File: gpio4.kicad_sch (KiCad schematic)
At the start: 4 parts, among them U27 RK3576

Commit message: Add files via upload
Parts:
- renumbered C330 to C102, C331 to C103, C332 to C104, U27 to U2

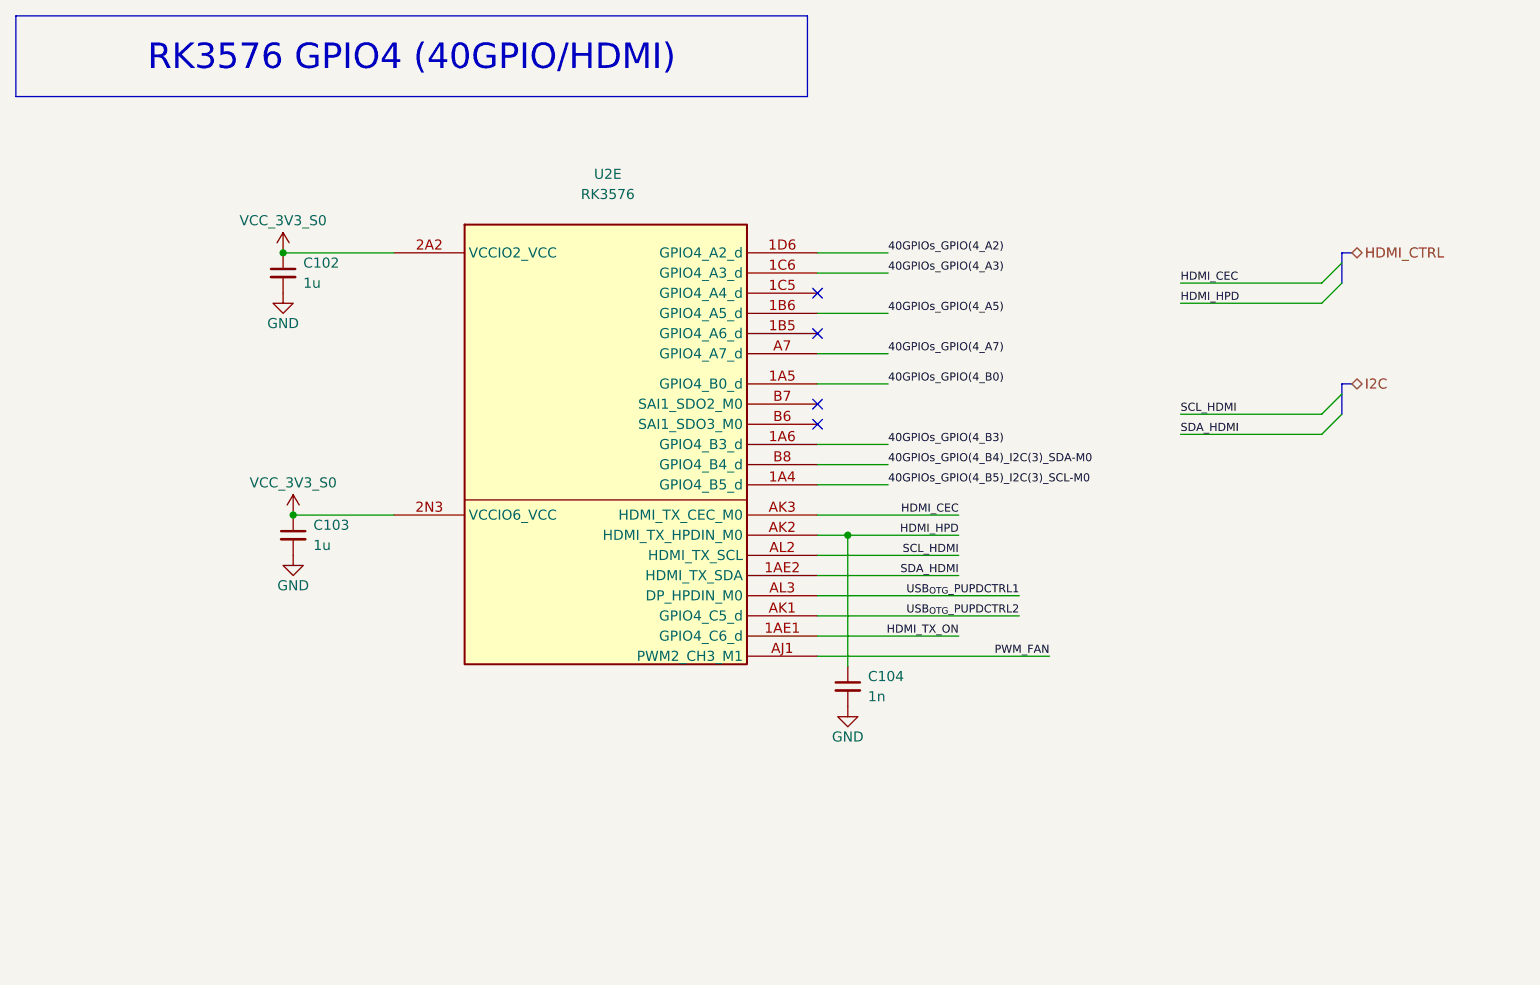
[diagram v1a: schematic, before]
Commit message: SBC Board V0.2
The SBC schematics before footprint and part number check
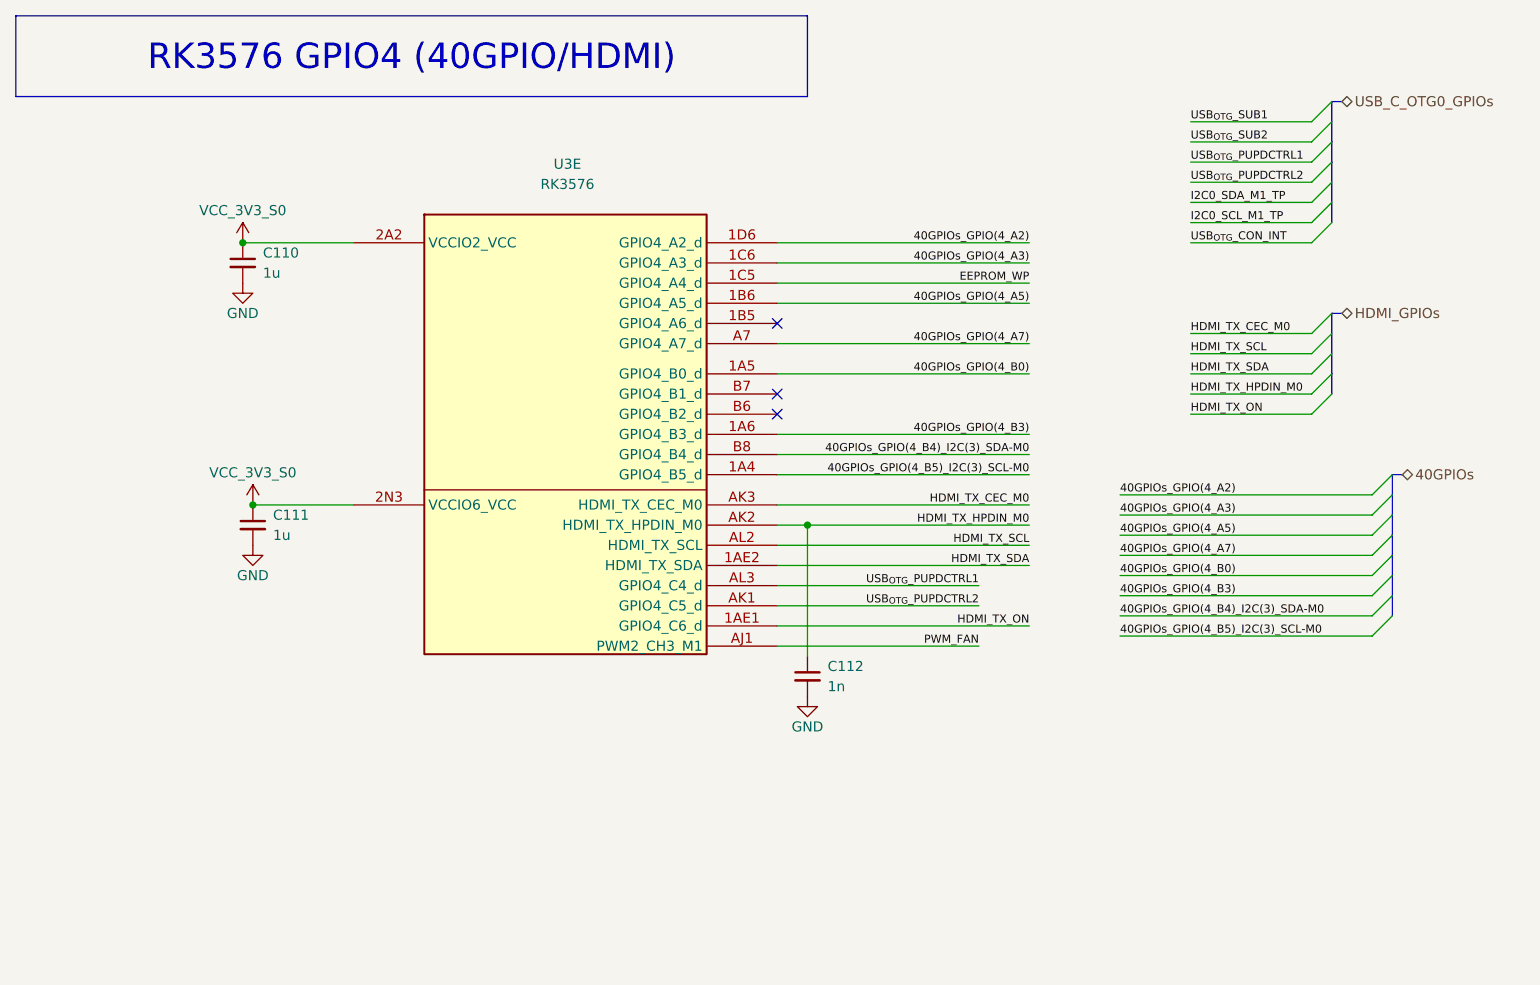
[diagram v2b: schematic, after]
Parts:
- U3: renamed from U2; footprint (none) -> easyeda2kicad:FCCSP-698_L17.2-W16.1-TL_RK3576
- renumbered C102 to C110, C103 to C111, C104 to C112
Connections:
- net EEPROM_WP: now reaches U3.1C5 (SAI4_SCLK_M0)
- net HDMI_CEC renamed HDMI_TX_CEC_M0
- net HDMI_HPD renamed HDMI_TX_HPDIN_M0
- net SCL_HDMI renamed HDMI_TX_SCL
- net SDA_HDMI renamed HDMI_TX_SDA
- no-connect marks 4 -> 3
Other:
- moved on the sheet: C110, C111, C112, U3E

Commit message: SBCv0.3
there is no big thing update just some LCSC & Mouser parts
and Big problem deleted alot of component values (:
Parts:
- removed C112: 1n, Capacitor_SMD:C_0402_1005Metric_Pad0.74x0.62mm_HandSolder, symbol New_Library_0:C_Small_edited
- added C398: 10n, Capacitor_SMD:C_0201_0603Metric_Pad0.64x0.40mm_HandSolder, symbol New_Library_0:C_Small_edited
- C110, C111: footprint Capacitor_SMD:C_0402_1005Metric_Pad0.74x0.62mm_HandSolder -> Capacitor_SMD:C_0201_0603Metric_Pad0.64x0.40mm_HandSolder; LCSC Part (none) -> C5209398; Mouser Part (none) -> CL03A105KP3NSNC
- U3: value RK3576 -> (none); LCSC Part (none) -> (polyline
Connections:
- net GND: now also C398.2
- net HDMI_TX_HPDIN_M0: now also C398.1
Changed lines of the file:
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@@
-	)
-	(symbol
-		(lib_id "New_Library_0:C_Small_edited")
-		(at 111.76 95.25 0)
-		(unit 1)
-		(body_style 1)
-		(exclude_from_sim no)
-		(in_bom yes)
-		(on_board yes)
-		(in_pos_files yes)
-		(dnp no)
-		(fields_autoplaced yes)
-		(property "Reference" "C112"
-			(at 114.3 93.9862 0)
-			(show_name no)
-			(do_not_autoplace no)
-			(effects
-				(font
-					(size 1.27 1.27)
-				)
-				(justify left)
-			)
-		)
-		(property "Value" "1n"
-			(at 114.3 96.5262 0)
-			(show_name no)
-			(do_not_autoplace no)
-			(effects
-				(font
-					(size 1.27 1.27)
-				)
-				(justify left)
-			)
-		)
-		(property "Footprint" "Capacitor_SMD:C_0402_1005Metric_Pad0.74x0.62mm_HandSolder"
-			(at 111.76 95.25 0)
-			(hide yes)
-			(show_name no)
-			(do_not_autoplace no)
-			(effects
-				(font
-					(size 1.27 1.27)
-				)
-			)
-		)
-		(property "Datasheet" ""
-			(at 111.76 95.25 0)
-			(hide yes)
-			(show_name no)
-			(do_not_autoplace no)
-			(effects
-				(font
-					(size 1.27 1.27)
-				)
-			)
-		)
-		(property "Description" "Unpolarized capacitor, small symbol"
-			(at 111.76 95.25 0)
-			(hide yes)
-			(show_name no)
-			(do_not_autoplace no)
-			(effects
-				(font
-					(size 1.27 1.27)
-				)
-			)
-		)
-		(property "Dielectric" ""
-			(at 111.76 95.25 0)
-			(hide yes)
-			(show_name no)
-			(do_not_autoplace no)
-			(effects
-				(font
-					(size 1.27 1.27)
-				)
-			)
-		)
-		(property "Voltage" ""
-			(at 111.76 95.25 0)
-			(hide yes)
-			(show_name no)
-			(do_not_autoplace no)
-			(effects
-				(font
-					(size 1.27 1.27)
-				)
-			)
-		)
-		(property "KLC_S3.3" ""
-			(at 111.76 95.25 0)
-			(hide yes)
-			(show_name no)
-			(do_not_autoplace no)
-			(effects
-				(font
-					(size 1.27 1.27)
-				)
-			)
-		)
-		(property "KLC_S4.1" ""
-			(at 111.76 95.25 0)
-			(hide yes)
-			(show_name no)
-			(do_not_autoplace no)
-			(effects
-				(font
-					(size 1.27 1.27)
-				)
-			)
-		)
-		(property "KLC_S5.1" ""
-			(at 111.76 95.25 0)
-			(hide yes)
-			(show_name no)
-			(do_not_autoplace no)
-			(effects
-				(font
-					(size 1.27 1.27)
-				)
-			)
-		)
-		(pin "1"
-		)
-		(pin "2"
-		)
-		(instances
-			(project "RK3576 SBC"
-				(path "/b79dbff4-0cad-4ff7-bec2-7c0e4f8b14d3/34f9b0cb-aeae-42b4-a2af-a0a79afcf392/3a63a63f-0660-4de2-bd2e-c637401ccb58"
-					(reference "C112")
-					(unit 1)
-				)
-			)
-		)
 	)
 	(symbol
@@
 			)
 		)
-		(property "Value" "RK3576"
+		(property "Value" ""
 			(at 81.534 33.274 0)
 			(show_name no)
@@
 			)
 		)
-		(property "KLC_S5.1" ""
+		(property "LCSC Part" "(polyline"
+			(at 81.28 64.77 0)
+			(hide yes)
+			(show_name no)
+			(do_not_autoplace no)
+			(effects
+				(font
+					(size 1.27 1.27)
+				)
+			)
+		)
+		(property "KLC_S4.2_DVDD" ""
+			(at 81.28 64.77 0)
+			(hide yes)
+			(show_name no)
+			(do_not_autoplace no)
+			(effects
+				(font
+					(size 1.27 1.27)
+				)
+			)
+		)
+		(property "KLC_S4.2_VREG_LX" ""
 			(at 81.28 64.77 0)
 			(hide yes)
@@
 					(reference "U3")
 					(unit 5)
+					(variant
+						(name "Test")
+					)
 				)
 			)
@@
 					(reference "#PWR0154")
 					(unit 1)
+				)
+			)
+		)
+	)
+	(symbol
+		(lib_id "New_Library_0:C_Small_edited")
+		(at 111.76 95.25 0)
+		(unit 1)
+		(body_style 1)
+		(exclude_from_sim no)
+		(in_bom yes)
+		(on_board yes)
+		(in_pos_files yes)
+		(dnp no)
+		(property "Reference" "C398"
+			(at 114.3 93.9862 0)
+			(show_name no)
+			(do_not_autoplace no)
+			(effects
+				(font
+					(size 1.27 1.27)
+				)
+				(justify left)
+			)
+		)
+		(property "Value" "10n"
+			(at 114.3 96.5262 0)
+			(show_name no)
+			(do_not_autoplace no)
+			(effects
+				(font
+					(size 1.27 1.27)
+				)
+				(justify left)
+			)
+		)
+		(property "Footprint" "Capacitor_SMD:C_0201_0603Metric_Pad0.64x0.40mm_HandSolder"
+			(at 111.76 95.25 0)
+			(hide yes)
+			(show_name no)
+			(do_not_autoplace no)
+			(effects
+				(font
+					(size 1.27 1.27)
+				)
+			)
+		)
+		(property "Datasheet" ""
+			(at 111.76 95.25 0)
+			(hide yes)
+			(show_name no)
+			(do_not_autoplace no)
+			(effects
+				(font
+					(size 1.27 1.27)
+				)
+			)
+		)
+		(property "Description" "Unpolarized capacitor, small symbol"
+			(at 111.76 95.25 0)
+			(hide yes)
+			(show_name no)
+			(do_not_autoplace no)
+			(effects
+				(font
+					(size 1.27 1.27)
+				)
+			)
+		)
+		(property "Dielectric" ""
+			(at 111.76 95.25 0)
+			(hide yes)
+			(show_name no)
+			(do_not_autoplace no)
+			(effects
+				(font
+					(size 1.27 1.27)
+				)
+			)
+		)
+		(property "Voltage" ""
+			(at 111.76 95.25 0)
+			(hide yes)
+			(show_name no)
+			(do_not_autoplace no)
+			(effects
+				(font
+					(size 1.27 1.27)
+				)
+			)
+		)
+		(property "LCSC Part" "C87461"
+			(at 111.76 95.25 0)
+			(hide yes)
+			(show_name no)
+			(do_not_autoplace no)
+			(effects
+				(font
+					(size 1.27 1.27)
+				)
+			)
+		)
+		(property "Mouser Part" "187-CL03B103KP3NNNC "
+			(at 111.76 95.25 0)
+			(hide yes)
+			(show_name no)
+			(do_not_autoplace no)
+			(effects
+				(font
+					(size 1.27 1.27)
+				)
+			)
+		)
+		(property "KLC_S3.3" ""
+			(at 111.76 95.25 0)
+			(hide yes)
+			(show_name no)
+			(do_not_autoplace no)
+			(effects
+				(font
+					(size 1.27 1.27)
+				)
+			)
+		)
+		(property "KLC_S4.1" ""
+			(at 111.76 95.25 0)
+			(hide yes)
+			(show_name no)
+			(do_not_autoplace no)
+			(effects
+				(font
+					(size 1.27 1.27)
+				)
+			)
+		)
+		(property "KLC_S4.2_DVDD" ""
+			(at 111.76 95.25 0)
+			(hide yes)
+			(show_name no)
+			(do_not_autoplace no)
+			(effects
+				(font
+					(size 1.27 1.27)
+				)
+			)
+		)
+		(property "KLC_S4.2_VREG_LX" ""
+			(at 111.76 95.25 0)
+			(hide yes)
+			(show_name no)
+			(do_not_autoplace no)
+			(effects
+				(font
+					(size 1.27 1.27)
+				)
+			)
+		)
+		(pin "1"
+		)
+		(pin "2"
+		)
+		(instances
+			(project "RK3576 SBC"
+				(path "/b79dbff4-0cad-4ff7-bec2-7c0e4f8b14d3/34f9b0cb-aeae-42b4-a2af-a0a79afcf392/3a63a63f-0660-4de2-bd2e-c637401ccb58"
+					(reference "C398")
+					(unit 1)
+					(variant
+						(name "Test")
+					)
 				)
 			)
@@
 			)
 		)
-		(property "Footprint" "Capacitor_SMD:C_0402_1005Metric_Pad0.74x0.62mm_HandSolder"
+		(property "Footprint" "Capacitor_SMD:C_0201_0603Metric_Pad0.64x0.40mm_HandSolder"
 			(at 41.91 76.2 0)
 			(hide yes)
@@
 			)
 		)
-		(property "KLC_S5.1" ""
+		(property "LCSC Part" "C5209398"
+			(at 41.91 76.2 0)
+			(hide yes)
+			(show_name no)
+			(do_not_autoplace no)
+			(effects
+				(font
+					(size 1.27 1.27)
+				)
+			)
+		)
+		(property "Mouser Part" "CL03A105KP3NSNC "
+			(at 41.91 76.2 0)
+			(hide yes)
+			(show_name no)
+			(do_not_autoplace no)
+			(effects
+				(font
+					(size 1.27 1.27)
+				)
+			)
+		)
+		(property "KLC_S4.2_DVDD" ""
+			(at 41.91 76.2 0)
+			(hide yes)
+			(show_name no)
+			(do_not_autoplace no)
+			(effects
+				(font
+					(size 1.27 1.27)
+				)
+			)
+		)
+		(property "KLC_S4.2_VREG_LX" ""
 			(at 41.91 76.2 0)
 			(hide yes)
@@
 					(reference "C111")
 					(unit 1)
+					(variant
+						(name "Test")
+					)
 				)
 			)
@@
 			)
 		)
-		(property "Footprint" "Capacitor_SMD:C_0402_1005Metric_Pad0.74x0.62mm_HandSolder"
+		(property "Footprint" "Capacitor_SMD:C_0201_0603Metric_Pad0.64x0.40mm_HandSolder"
 			(at 40.64 43.18 0)
 			(hide yes)
@@
 			)
 		)
-		(property "KLC_S5.1" ""
+		(property "LCSC Part" "C5209398"
+			(at 40.64 43.18 0)
+			(hide yes)
+			(show_name no)
+			(do_not_autoplace no)
+			(effects
+				(font
+					(size 1.27 1.27)
+				)
+			)
+		)
+		(property "Mouser Part" "CL03A105KP3NSNC "
+			(at 40.64 43.18 0)
+			(hide yes)
+			(show_name no)
+			(do_not_autoplace no)
+			(effects
+				(font
+					(size 1.27 1.27)
+				)
+			)
+		)
+		(property "KLC_S4.2_DVDD" ""
+			(at 40.64 43.18 0)
+			(hide yes)
+			(show_name no)
+			(do_not_autoplace no)
+			(effects
+				(font
+					(size 1.27 1.27)
+				)
+			)
+		)
+		(property "KLC_S4.2_VREG_LX" ""
 			(at 40.64 43.18 0)
 			(hide yes)
@@
 					(reference "C110")
 					(unit 1)
-				)
-			)
+					(variant
+						(name "Test")
+					)
+				)
+			)

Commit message: SBCv0.4
add LCSC & Mouser parts 
and solve the deleted value in the past version
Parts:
- added C200: 1u, Capacitor_SMD:C_0201_0603Metric_Pad0.64x0.40mm_HandSolder, symbol New_Library_0:C_Small_edited
- added U1: M24C64-RMN6TP, Package_SO:SOIC-8_3.9x4.9mm_P1.27mm, symbol Memory_NVRAM:FM24C64B
- U3: value (none) -> RK3576; LCSC Part (polyline -> C42388007
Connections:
- net EEPROM_WP: now also U1.7 (WP)
- net GND: now also C200.2, U1.1 (A0), U1.2 (A1), U1.3 (A2), U1.4 (VSS)
- new net I2C2_SCL_M0_CC_RTC_EEPROM: U1.6 (SCL)
- new net I2C2_SDA_M0_CC_RTC_EEPROM: U1.5 (SDA)
- new net VCC_3.3v_S0: C200.1, U1.8 (VDD)

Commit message: SBCv0.5
small update for Josa watch the final version
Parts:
- removed C200: 1u, Capacitor_SMD:C_0201_0603Metric_Pad0.64x0.40mm_HandSolder, symbol New_Library_0:C_Small_edited
- removed U1: M24C64-RMN6TP, Package_SO:SOIC-8_3.9x4.9mm_P1.27mm, symbol Memory_NVRAM:FM24C64B
